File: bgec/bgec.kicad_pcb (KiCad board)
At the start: 4 copper layers, 10 parts

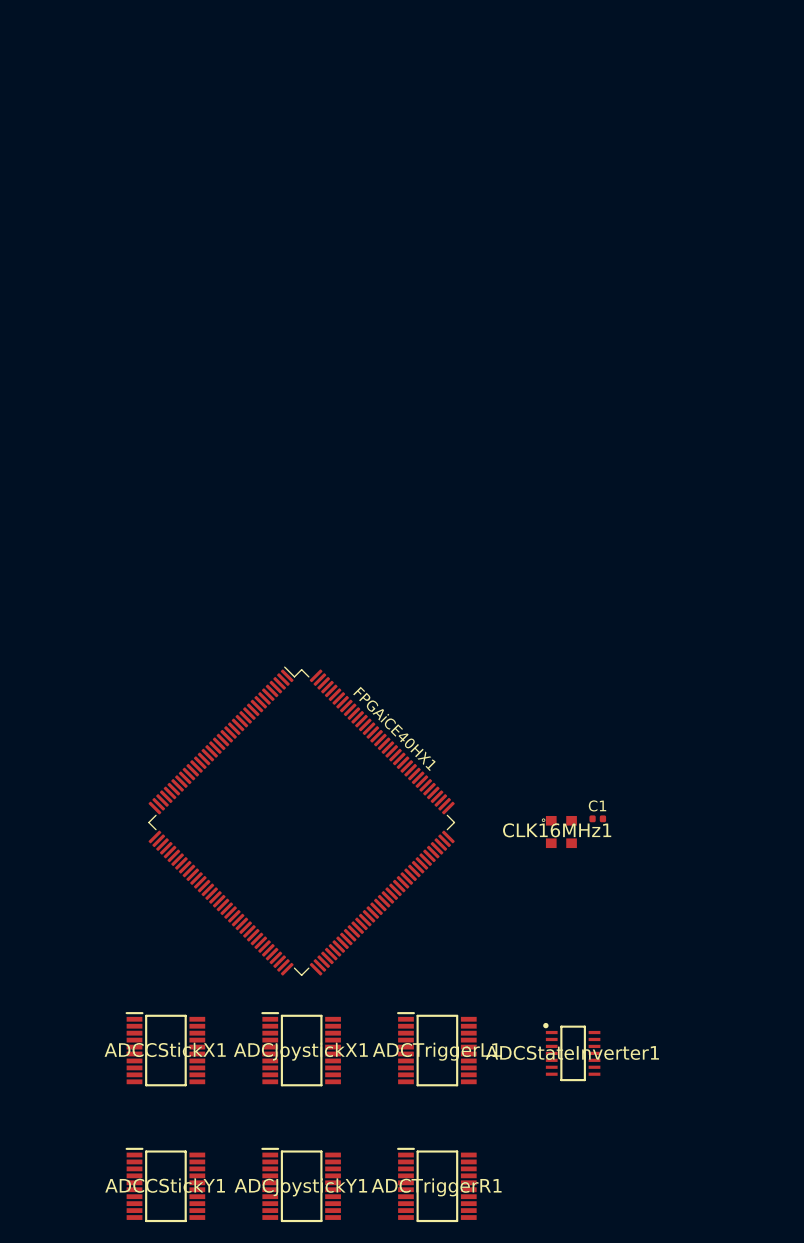
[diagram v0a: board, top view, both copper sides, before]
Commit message: Properly feed all ADC pins to the FPGA
Includes rudimentary routing. In the future I'm definitely going to move the ADCs closer to their joysticks/triggers so the model doesn't look like a swastika.
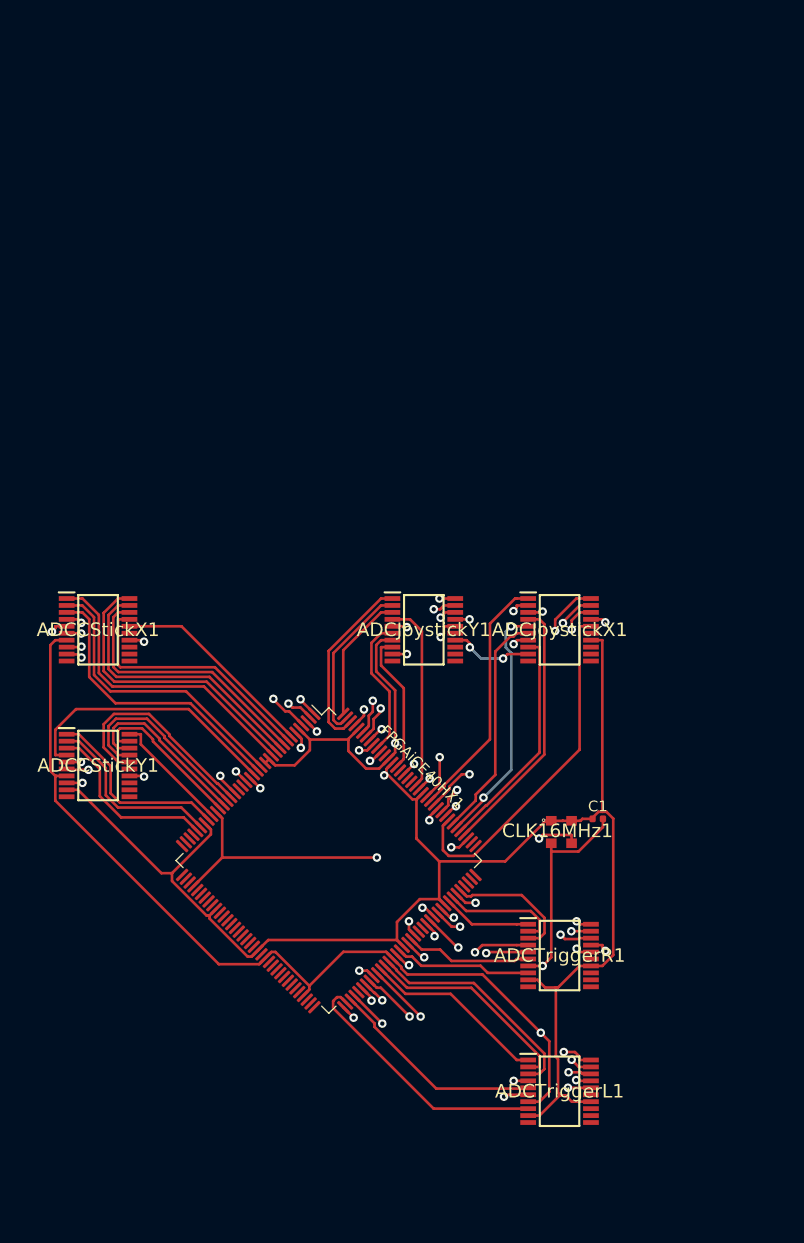
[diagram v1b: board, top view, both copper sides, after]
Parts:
- removed ADCStateInverter1: 74HC04, LibraryLoader:SON65P440X500X110-14N
- moved ADCJoystickY1 53.3 mm to (148.6, 92.7)
- moved ADCJoystickX1 46.2 mm to (161.3, 92.7)
- moved ADCCStickX1 39.9 mm to (118.1, 92.7)
- moved ADCCStickY1 39.9 mm to (118.1, 105.4)
- moved ADCTriggerR1 24.4 mm to (161.3, 123.2)
- moved ADCTriggerL1 12.0 mm to (161.3, 135.9)
- moved FPGAiCE40HX1 4.37 mm to (139.7, 114.3)
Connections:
- ADCCStickX1 pad 4: Net-(ADCCStickX1-Pad4) -> CStickXNotCONVST
- ADCCStickX1 pad 5: Net-(ADCCStickX1-Pad5) -> CStickXNotCS
- ADCCStickX1 pad 6: Net-(ADCCStickX1-Pad6) -> CStickXNotRD
- ADCCStickX1 pad 9: Net-(ADCCStickX1-Pad9) -> GCLogic
- ADCCStickY1 pad 4: Net-(ADCCStickY1-Pad4) -> CStickYNotCONVST
- ADCCStickY1 pad 5: Net-(ADCCStickY1-Pad5) -> CStickYNotCS
- ADCCStickY1 pad 6: Net-(ADCCStickY1-Pad6) -> CStickYNotRD
- ADCCStickY1 pad 9: Net-(ADCCStickY1-Pad9) -> GCLogic
- ADCJoystickX1 pad 4: Net-(ADCJoystickX1-Pad4) -> JoystickXNotCONVST
- ADCJoystickX1 pad 5: Net-(ADCJoystickX1-Pad5) -> JoystickXNotCS
- ADCJoystickX1 pad 6: Net-(ADCJoystickX1-Pad6) -> JoystickXNotRD
- ADCJoystickX1 pad 9: Net-(ADCJoystickX1-Pad9) -> GCLogic
- ADCJoystickY1 pad 4: Net-(ADCJoystickY1-Pad4) -> JoystickYNotCONVST
- ADCJoystickY1 pad 5: Net-(ADCJoystickY1-Pad5) -> JoystickYNotCS
- ADCJoystickY1 pad 6: Net-(ADCJoystickY1-Pad6) -> JoystickYNotRD
- ADCJoystickY1 pad 9: Net-(ADCJoystickY1-Pad9) -> GCLogic
- ADCTriggerL1 pad 4: Net-(ADCTriggerL1-Pad4) -> TriggerLNotCONVST
- ADCTriggerL1 pad 5: Net-(ADCTriggerL1-Pad5) -> TriggerLNotCS
- ADCTriggerL1 pad 6: Net-(ADCTriggerL1-Pad6) -> TriggerLNotRD
- ADCTriggerL1 pad 9: Net-(ADCTriggerL1-Pad9) -> GCLogic
- ADCTriggerR1 pad 4: Net-(ADCTriggerR1-Pad4) -> TriggerRNotCONVST
- ADCTriggerR1 pad 5: Net-(ADCTriggerR1-Pad5) -> TriggerRNotCS
- ADCTriggerR1 pad 6: Net-(ADCTriggerR1-Pad6) -> TriggerRNotRD
- ADCTriggerR1 pad 9: Net-(ADCTriggerR1-Pad9) -> GCLogic
- FPGAiCE40HX1 pad 1: Net-(FPGAiCE40HX1-Pad1) -> CStickXNotCONVST
- FPGAiCE40HX1 pad 10: CStickXDB2 -> CStickXDB4
- FPGAiCE40HX1 pad 101: TriggerRDB4 -> TriggerRDB2
- FPGAiCE40HX1 pad 102: TriggerRDB3 -> TriggerRDB1
- FPGAiCE40HX1 pad 103: Net-(FPGAiCE40HX1-Pad103) -> GCLogicGround
- FPGAiCE40HX1 pad 104: TriggerRDB2 -> TriggerRDB0
- FPGAiCE40HX1 pad 105: TriggerRDB1 -> Net-(FPGAiCE40HX1-Pad105)
- FPGAiCE40HX1 pad 106: TriggerRDB0 -> Net-(FPGAiCE40HX1-Pad106)
- FPGAiCE40HX1 pad 11: CStickXDB1 -> CStickXDB3
- FPGAiCE40HX1 pad 112: Net-(FPGAiCE40HX1-Pad112) -> JoystickXNotCONVST
- FPGAiCE40HX1 pad 113: JoystickXEOC -> JoystickXNotEOC
- FPGAiCE40HX1 pad 114: JoystickXDB7 -> JoystickXNotCS
- FPGAiCE40HX1 pad 115: JoystickXDB6 -> JoystickXNotRD
- FPGAiCE40HX1 pad 116: JoystickXDB5 -> JoystickXDB7
- FPGAiCE40HX1 pad 117: JoystickXDB4 -> JoystickXDB6
- FPGAiCE40HX1 pad 118: JoystickXDB3 -> JoystickXDB5
- FPGAiCE40HX1 pad 119: JoystickXDB2 -> JoystickXDB4
- FPGAiCE40HX1 pad 12: CStickXDB0 -> CStickXDB2
- FPGAiCE40HX1 pad 120: JoystickXDB1 -> JoystickXDB3
- FPGAiCE40HX1 pad 121: JoystickXDB0 -> JoystickXDB2
- FPGAiCE40HX1 pad 122: Net-(FPGAiCE40HX1-Pad122) -> JoystickXDB1
- FPGAiCE40HX1 pad 124: Net-(FPGAiCE40HX1-Pad124) -> JoystickXDB0
- FPGAiCE40HX1 pad 125: Net-(FPGAiCE40HX1-Pad125) -> JoystickYNotCONVST
- FPGAiCE40HX1 pad 13: Net-(FPGAiCE40HX1-Pad103) -> GCLogicGround
- FPGAiCE40HX1 pad 130: Net-(FPGAiCE40HX1-Pad130) -> JoystickYNotEOC
- FPGAiCE40HX1 pad 132: Net-(FPGAiCE40HX1-Pad103) -> GCLogicGround
- FPGAiCE40HX1 pad 134: JoystickYEOC -> JoystickYNotCS
- FPGAiCE40HX1 pad 135: JoystickYDB7 -> JoystickYNotRD
- FPGAiCE40HX1 pad 136: JoystickYDB6 -> JoystickYDB7
- FPGAiCE40HX1 pad 137: JoystickYDB5 -> JoystickYDB6
- FPGAiCE40HX1 pad 138: JoystickYDB4 -> JoystickYDB5
- FPGAiCE40HX1 pad 139: JoystickYDB3 -> JoystickYDB4
- FPGAiCE40HX1 pad 14: Net-(FPGAiCE40HX1-Pad103) -> GCLogicGround
- FPGAiCE40HX1 pad 140: Net-(FPGAiCE40HX1-Pad103) -> GCLogicGround
- FPGAiCE40HX1 pad 141: JoystickYDB2 -> JoystickYDB3
- FPGAiCE40HX1 pad 142: JoystickYDB1 -> JoystickYDB2
- FPGAiCE40HX1 pad 143: JoystickYDB0 -> JoystickYDB1
- FPGAiCE40HX1 pad 144: Net-(FPGAiCE40HX1-Pad144) -> JoystickYDB0
- FPGAiCE40HX1 pad 15: Net-(FPGAiCE40HX1-Pad15) -> CStickXDB1
- FPGAiCE40HX1 pad 16: Net-(FPGAiCE40HX1-Pad16) -> CStickXDB0
- FPGAiCE40HX1 pad 17: Net-(FPGAiCE40HX1-Pad17) -> CStickYNotCONVST
- FPGAiCE40HX1 pad 18: Net-(FPGAiCE40HX1-Pad18) -> CStickYNotEOC
- FPGAiCE40HX1 pad 19: Net-(FPGAiCE40HX1-Pad19) -> CStickYNotCS
- FPGAiCE40HX1 pad 2: CStickXEOC -> CStickXNotEOC
- FPGAiCE40HX1 pad 22: Net-(FPGAiCE40HX1-Pad22) -> CStickYNotRD
- FPGAiCE40HX1 pad 23: CStickYEOC -> CStickYDB7
- FPGAiCE40HX1 pad 24: CStickYDB7 -> CStickYDB6
- FPGAiCE40HX1 pad 25: CStickYDB6 -> CStickYDB5
- FPGAiCE40HX1 pad 26: CStickYDB5 -> CStickYDB4
- FPGAiCE40HX1 pad 28: CStickYDB4 -> CStickYDB3
- FPGAiCE40HX1 pad 29: CStickYDB3 -> CStickYDB2
- FPGAiCE40HX1 pad 3: CStickXDB7 -> CStickXNotCS
- FPGAiCE40HX1 pad 31: CStickYDB2 -> CStickYDB1
- FPGAiCE40HX1 pad 32: CStickYDB1 -> CStickYDB0
- FPGAiCE40HX1 pad 33: CStickYDB0 -> Net-(FPGAiCE40HX1-Pad33)
- FPGAiCE40HX1 pad 4: CStickXDB6 -> CStickXNotRD
- FPGAiCE40HX1 pad 5: Net-(FPGAiCE40HX1-Pad103) -> GCLogicGround
- FPGAiCE40HX1 pad 59: Net-(FPGAiCE40HX1-Pad103) -> GCLogicGround
- FPGAiCE40HX1 pad 69: Net-(FPGAiCE40HX1-Pad103) -> GCLogicGround
- FPGAiCE40HX1 pad 7: CStickXDB5 -> CStickXDB7
- FPGAiCE40HX1 pad 73: Net-(FPGAiCE40HX1-Pad73) -> TriggerLNotCONVST
- FPGAiCE40HX1 pad 74: TriggerLEOC -> TriggerLNotEOC
- FPGAiCE40HX1 pad 75: TriggerLDB7 -> TriggerLNotCS
- FPGAiCE40HX1 pad 76: TriggerLDB6 -> TriggerLNotRD
- FPGAiCE40HX1 pad 78: TriggerLDB5 -> TriggerLDB7
- FPGAiCE40HX1 pad 79: TriggerLDB4 -> TriggerLDB6
- FPGAiCE40HX1 pad 8: CStickXDB4 -> CStickXDB6
- FPGAiCE40HX1 pad 80: TriggerLDB3 -> TriggerLDB5
- FPGAiCE40HX1 pad 81: TriggerLDB2 -> TriggerLDB4
- FPGAiCE40HX1 pad 82: TriggerLDB1 -> TriggerLDB3
- FPGAiCE40HX1 pad 83: TriggerLDB0 -> TriggerLDB2
- FPGAiCE40HX1 pad 84: Net-(FPGAiCE40HX1-Pad84) -> TriggerLDB1
- FPGAiCE40HX1 pad 85: Net-(FPGAiCE40HX1-Pad85) -> TriggerLDB0
- FPGAiCE40HX1 pad 86: Net-(FPGAiCE40HX1-Pad103) -> GCLogicGround
- FPGAiCE40HX1 pad 87: Net-(FPGAiCE40HX1-Pad87) -> TriggerRNotCONVST
- FPGAiCE40HX1 pad 88: Net-(FPGAiCE40HX1-Pad88) -> TriggerRNotEOC
- FPGAiCE40HX1 pad 9: CStickXDB3 -> CStickXDB5
- FPGAiCE40HX1 pad 90: Net-(FPGAiCE40HX1-Pad90) -> TriggerRNotCS
- FPGAiCE40HX1 pad 91: Net-(FPGAiCE40HX1-Pad91) -> TriggerRNotRD
- FPGAiCE40HX1 pad 95: Net-(FPGAiCE40HX1-Pad95) -> TriggerRDB7
- FPGAiCE40HX1 pad 96: TriggerREOC -> TriggerRDB6
- FPGAiCE40HX1 pad 97: TriggerRDB7 -> TriggerRDB5
- FPGAiCE40HX1 pad 98: TriggerRDB6 -> TriggerRDB4
- FPGAiCE40HX1 pad 99: TriggerRDB5 -> TriggerRDB3
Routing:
- net GCLogic: track 0.00 -> 220.0 mm, vias 0 -> 8
- net GCLogicGround: track 0.00 -> 189.1 mm, vias 0 -> 5
- net Net-(FPGAiCE40HX1-Pad111): track 0.00 -> 39.1 mm, vias 0 -> 3
- net JoystickXDB7: track 0.00 -> 32.8 mm
- net CStickXNotCS: track 0.00 -> 32.1 mm, vias 0 -> 2
- net CStickXDB2: track 0.00 -> 28.6 mm
- net JoystickXDB4: track 0.00 -> 28.4 mm, vias 0 -> 2
- net CStickXDB3: track 0.00 -> 27.7 mm
- net CStickXDB1: track 0.00 -> 27.6 mm
- net CStickXDB0: track 0.00 -> 27.2 mm
- net TriggerLDB4: track 0.00 -> 27.0 mm, vias 0 -> 2
- net CStickXNotCONVST: track 0.00 -> 26.9 mm, vias 0 -> 2
- net JoystickXDB3: track 0.00 -> 26.6 mm, vias 0 -> 2
- net CStickXDB4: track 0.00 -> 26.5 mm
- net JoystickXDB6: track 0.00 -> 25.8 mm, vias 0 -> 2
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
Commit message: Remodel ADC placement, add USB-C connector
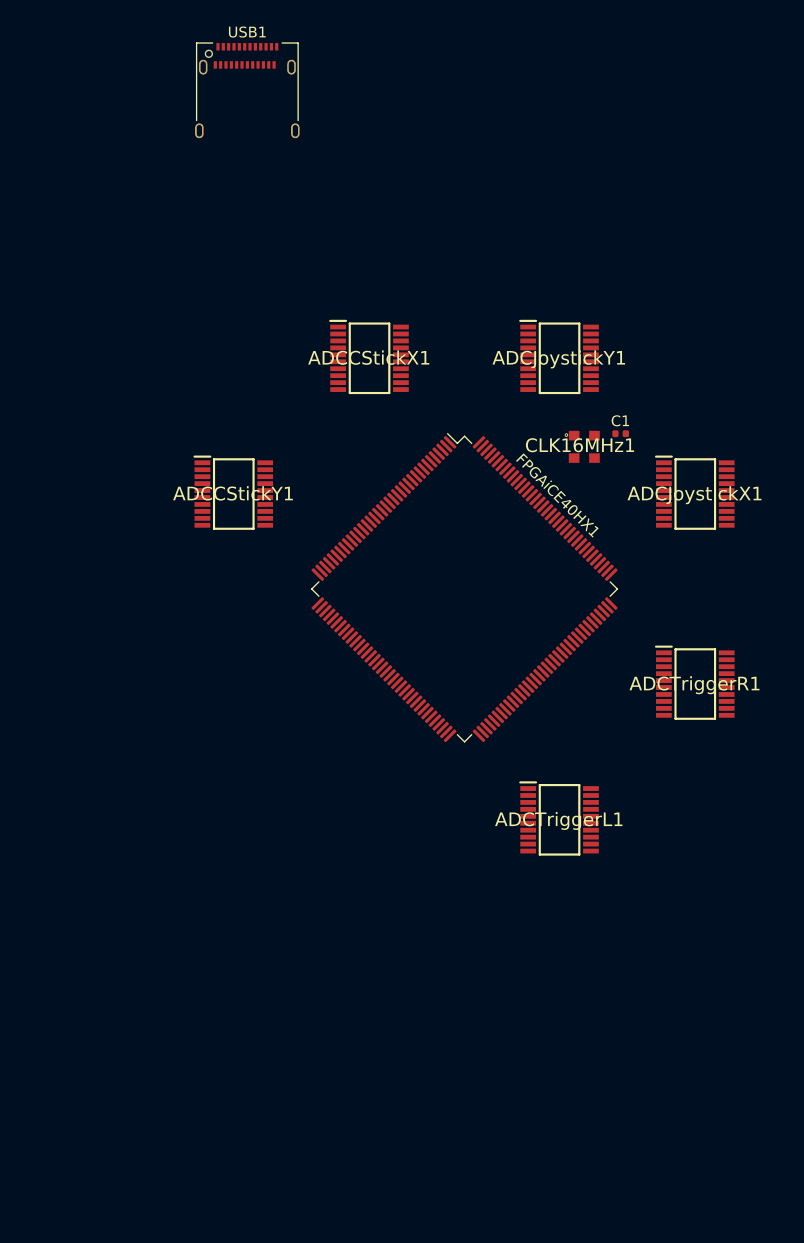
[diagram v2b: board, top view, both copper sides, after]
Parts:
- added USB1: USB_C_Receptacle, Connector_USB:USB_C_Receptacle_Amphenol_12401610E4-2A, F.Cu at (132.1, 43.2)
- moved CLK16MHz1 36.1 mm to (163.6, 75.6)
- moved C1 36.1 mm to (167.0, 74.4)
- moved ADCCStickX1 35.9 mm to (143.5, 67.3)
- moved ADCTriggerR1 28.4 mm to (174.0, 97.8)
- moved FPGAiCE40HX1 28.4 mm to (152.4, 88.9)
- moved ADCCStickY1 28.4 mm to (130.8, 80.0)
- moved ADCJoystickY1 28.4 mm to (161.3, 67.3)
- moved ADCTriggerL1 25.4 mm to (161.3, 110.5)
- moved ADCJoystickX1 18.0 mm to (174.0, 80.0)
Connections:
- FPGAiCE40HX1 pad 37: Net-(FPGAiCE40HX1-Pad37) -> USBData-
- FPGAiCE40HX1 pad 38: Net-(FPGAiCE40HX1-Pad38) -> USBData+
- FPGAiCE40HX1 pad 39: Net-(FPGAiCE40HX1-Pad39) -> USBRX1-
- FPGAiCE40HX1 pad 41: Net-(FPGAiCE40HX1-Pad41) -> USBRX1+
- FPGAiCE40HX1 pad 42: Net-(FPGAiCE40HX1-Pad42) -> USBTX1-
- FPGAiCE40HX1 pad 43: Net-(FPGAiCE40HX1-Pad43) -> USBTX1+
- FPGAiCE40HX1 pad 44: Net-(FPGAiCE40HX1-Pad44) -> USBRX2-
- FPGAiCE40HX1 pad 45: Net-(FPGAiCE40HX1-Pad45) -> USBRX2+
- FPGAiCE40HX1 pad 47: Net-(FPGAiCE40HX1-Pad47) -> USBTX2-
- FPGAiCE40HX1 pad 48: Net-(FPGAiCE40HX1-Pad48) -> USBTX2+
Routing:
- net GCLogic: track 220.0 -> 0.00 mm, vias 8 -> 0
- net GCLogicGround: track 189.1 -> 0.00 mm, vias 5 -> 0
- net Net-(FPGAiCE40HX1-Pad111): track 39.1 -> 0.00 mm, vias 3 -> 0
- net JoystickXDB7: track 32.8 -> 0.00 mm
- net CStickXNotCS: track 32.1 -> 0.00 mm, vias 2 -> 0
- net CStickXDB2: track 28.6 -> 0.00 mm
- net JoystickXDB4: track 28.4 -> 0.00 mm, vias 2 -> 0
- net CStickXDB3: track 27.7 -> 0.00 mm
- net CStickXDB1: track 27.6 -> 0.00 mm
- net CStickXDB0: track 27.2 -> 0.00 mm
- net TriggerLDB4: track 27.0 -> 0.00 mm, vias 2 -> 0
- net CStickXNotCONVST: track 26.9 -> 0.00 mm, vias 2 -> 0
- net JoystickXDB3: track 26.6 -> 0.00 mm, vias 2 -> 0
- net CStickXDB4: track 26.5 -> 0.00 mm
- net JoystickXDB6: track 25.8 -> 0.00 mm, vias 2 -> 0
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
